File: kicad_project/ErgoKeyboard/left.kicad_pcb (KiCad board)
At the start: 2 copper layers, 163.8 x 116.3 mm, 58 parts

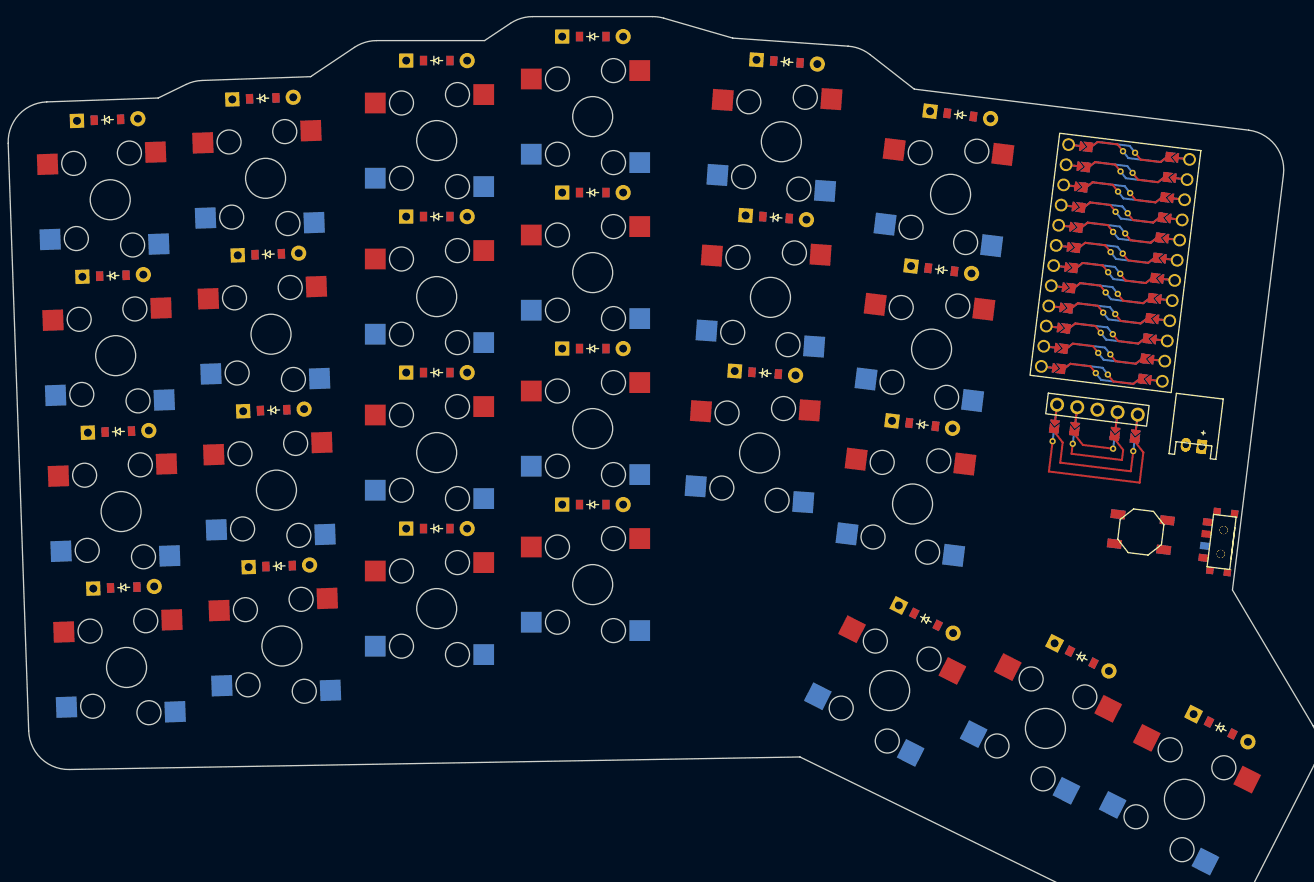
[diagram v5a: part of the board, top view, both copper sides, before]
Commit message: DRC doesn't like the smd trace hack, ouch
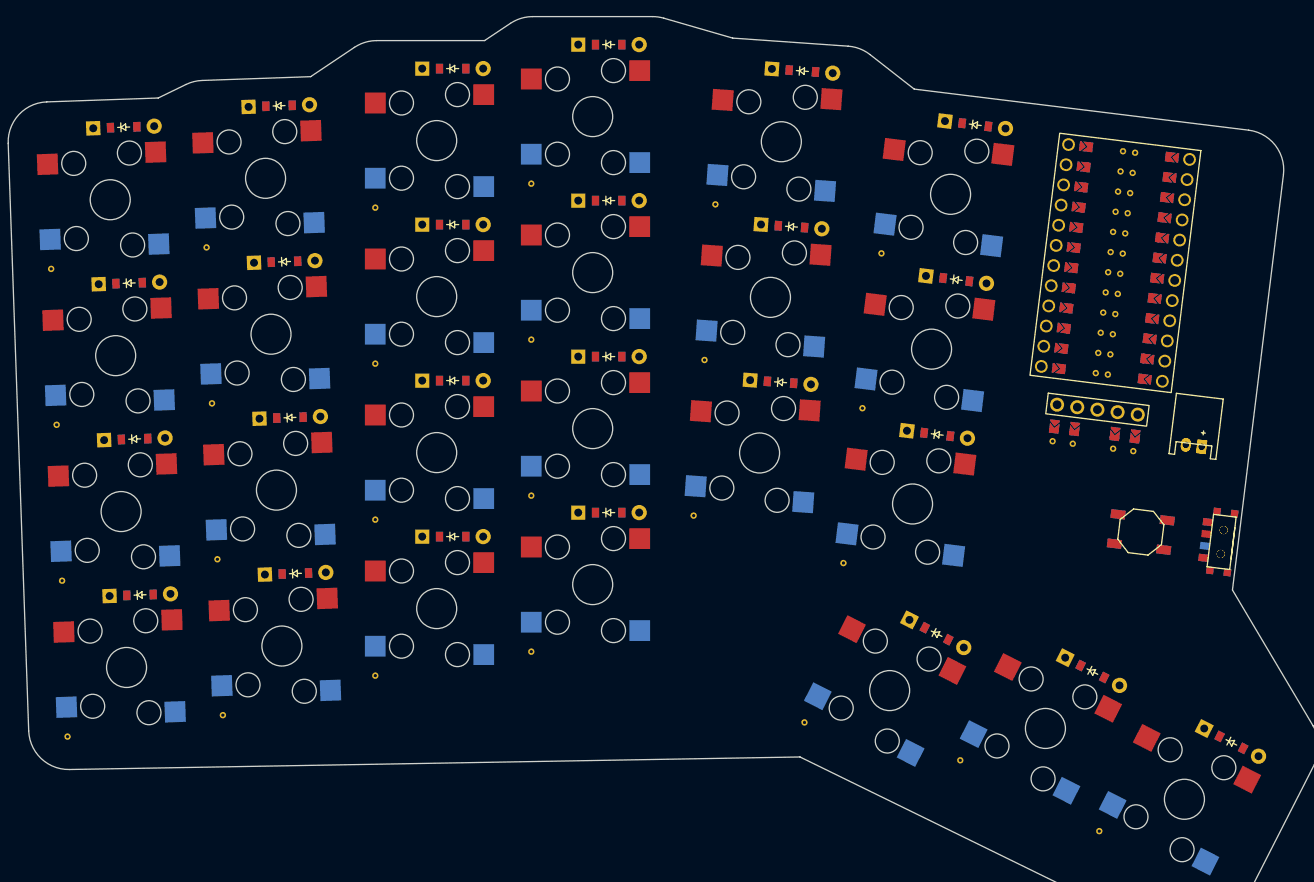
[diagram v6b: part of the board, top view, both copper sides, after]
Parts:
- moved D3 2.24 mm to (150.3, 127.0)
- moved D4 2.24 mm to (149.6, 107.5)
- moved D7 2.24 mm to (169.7, 124.3)
- moved D8 2.24 mm to (169.1, 104.8)
- moved D1 2.24 mm to (151.7, 165.9)
- moved D2 2.24 mm to (151.0, 146.4)
- moved D5 2.24 mm to (171.1, 163.3)
- moved D6 2.24 mm to (170.4, 143.8)
- moved D17 2.24 mm to (231.8, 139.4)
- moved D18 2.24 mm to (233.1, 119.9)
- moved D19 2.24 mm to (234.5, 100.4)
- moved D20 2.24 mm to (251.3, 145.9)
- moved D21 2.24 mm to (253.7, 126.5)
- moved D22 2.24 mm to (256.1, 107.2)
- moved D10 2.24 mm to (190.8, 139.1)
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
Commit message: using promicro pretty now, reverted some changes
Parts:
- MCU1: value rev_mcu -> (none); footprint revmicro -> ProMicro
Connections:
- MCU1 pad 1: P1 -> RAW
- MCU1 pad 10: P7 -> P14
- MCU1 pad 11: P8 -> P16
- MCU1 pad 12: P9 -> P10
- MCU1 pad 13: P10 -> P9
- MCU1 pad 14: P16 -> P8
- MCU1 pad 15: P14 -> P7
- MCU1 pad 16: P15 -> P6
- MCU1 pad 17: P18 -> P5
- MCU1 pad 18: P19 -> P4
- MCU1 pad 19: P20 -> P3
- MCU1 pad 2: P0 -> GND
- MCU1 pad 20: P21 -> P2
- MCU1 pad 21: VCC -> GND
- MCU1 pad 22: RST -> GND
- MCU1 pad 23: GND -> P0
- MCU1 pad 24: RAW -> P1
- MCU1 pad 3: GND -> RST
- MCU1 pad 4: GND -> VCC
- MCU1 pad 5: P2 -> P21
- MCU1 pad 6: P3 -> P20
- MCU1 pad 7: P4 -> P19
- MCU1 pad 8: P5 -> P18
- MCU1 pad 9: P6 -> P15

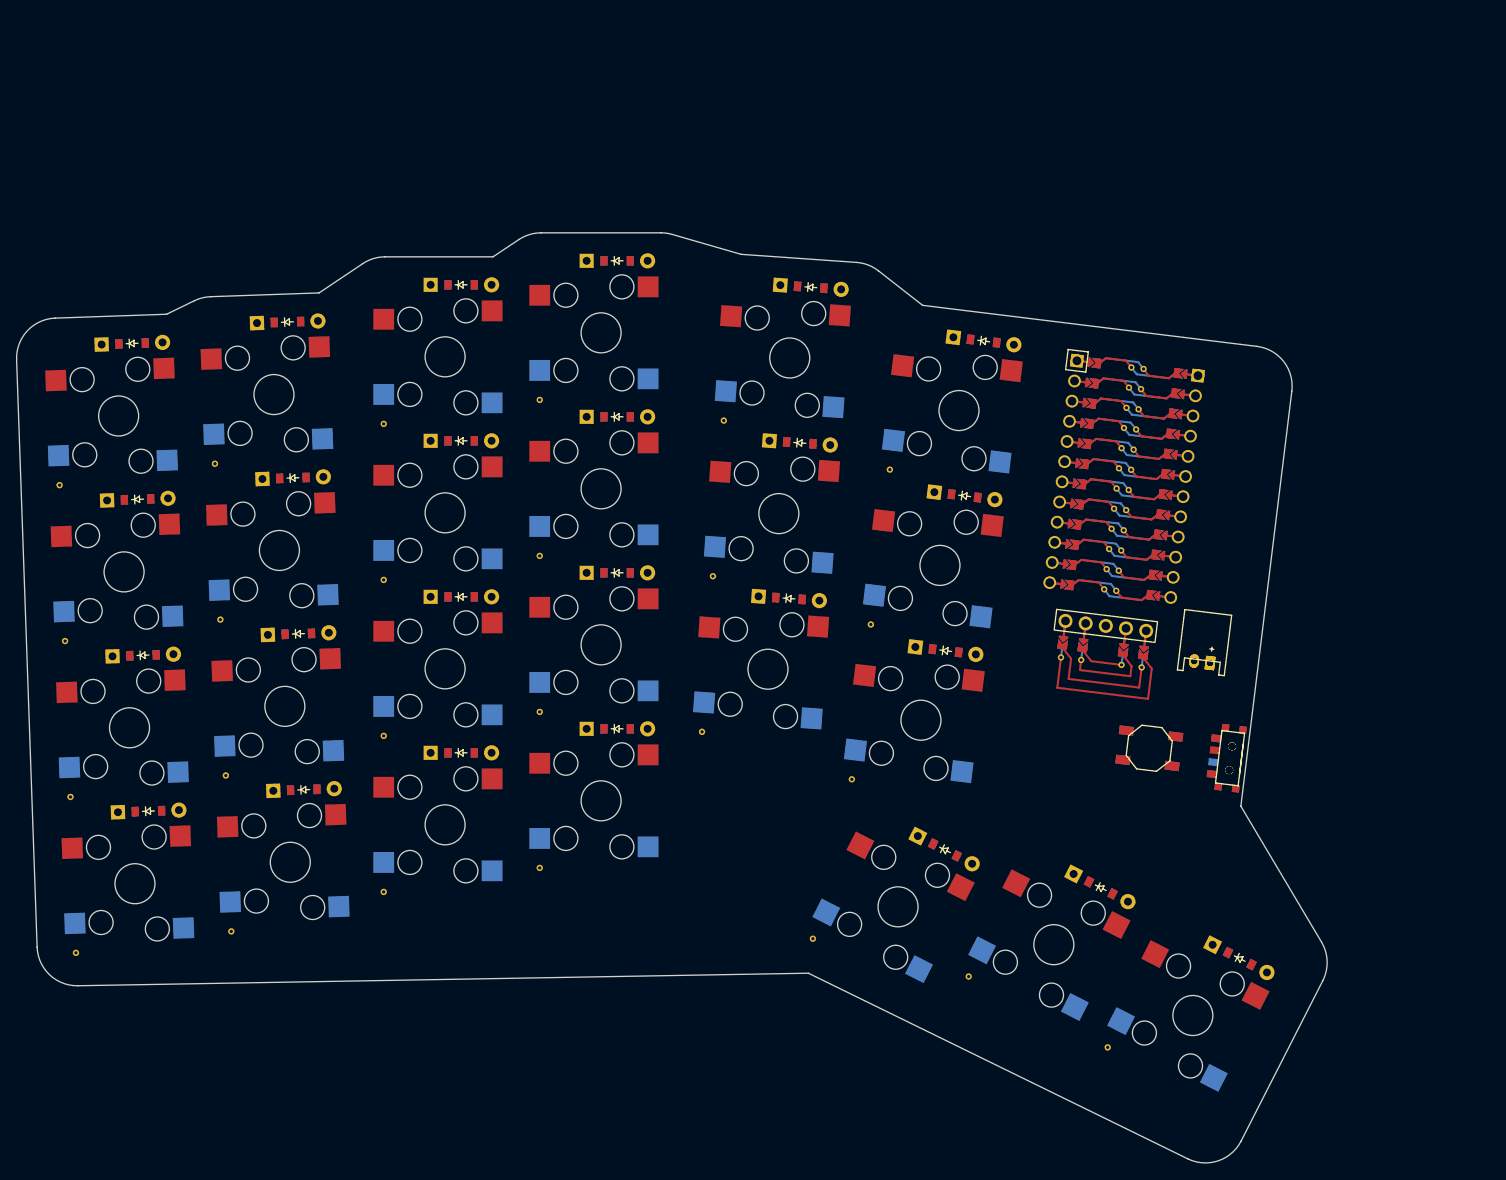
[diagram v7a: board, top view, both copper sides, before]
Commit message: niceview reworked to "pretty" method
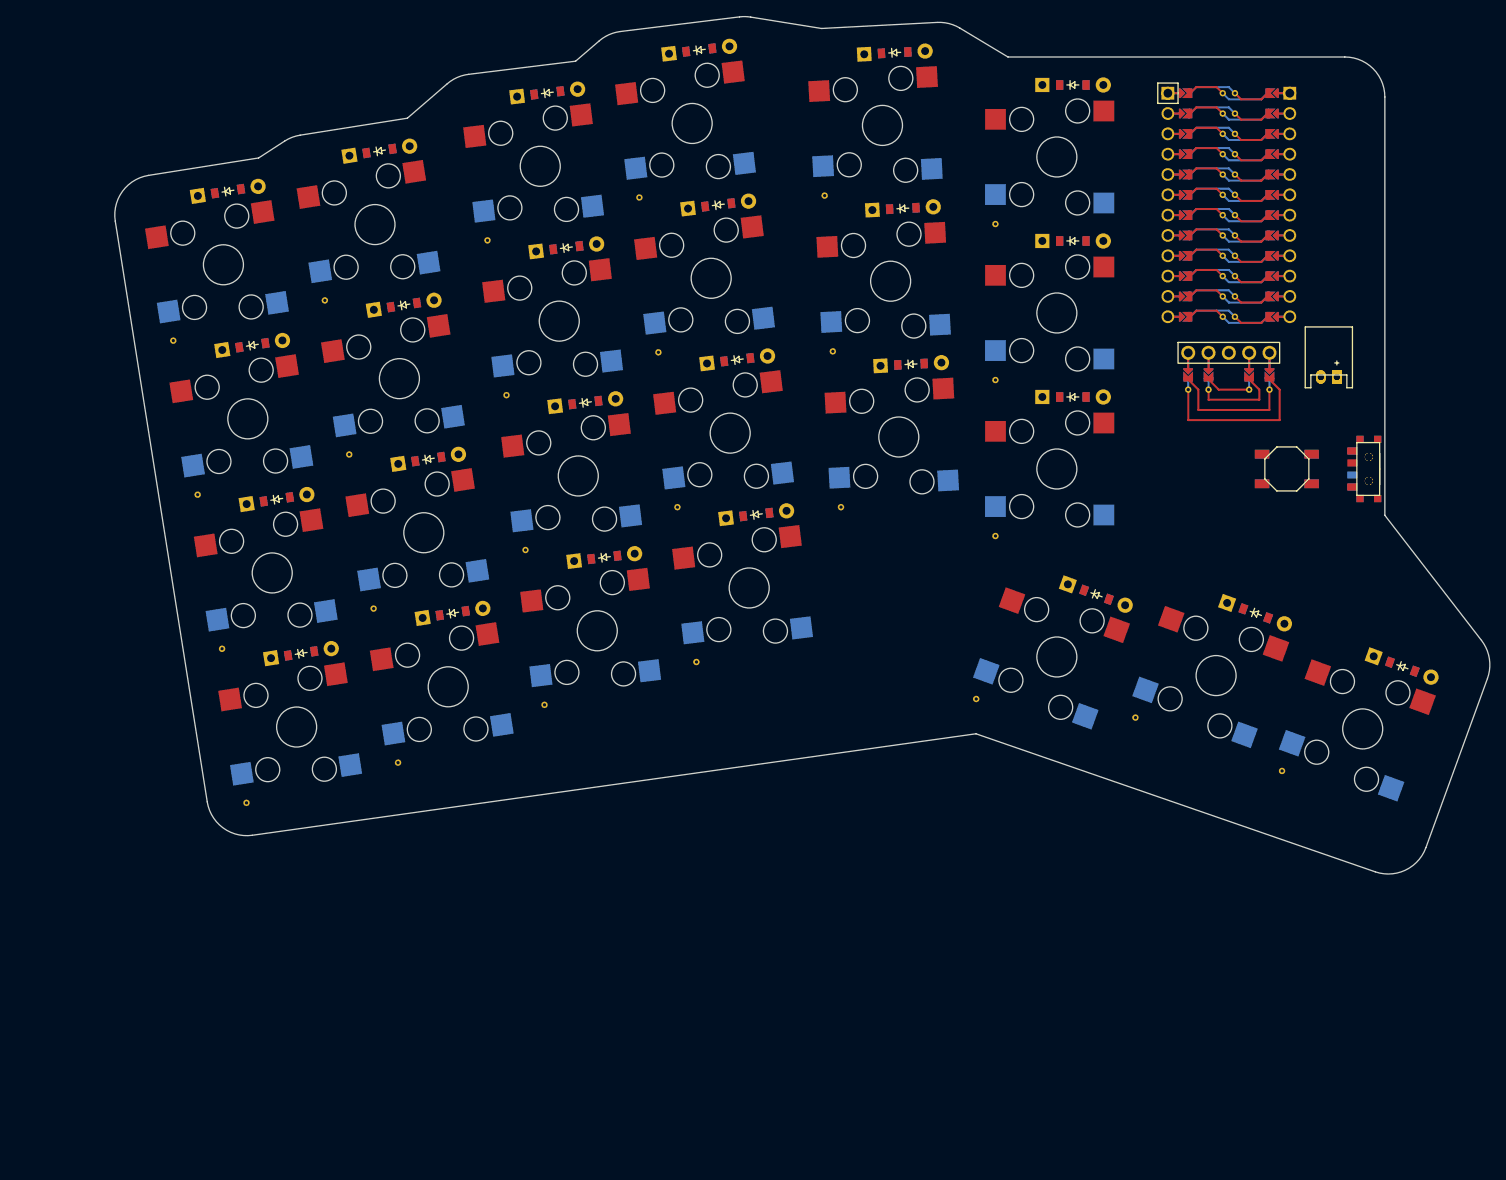
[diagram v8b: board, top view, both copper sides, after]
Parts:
- moved D25 41.8 mm to (308.4, 147.9), turned to -20 degrees
- moved S25 41.6 mm to (303.5, 155.7), turned to -20 degrees
- moved T1 40.1 mm to (304.2, 123.2), turned to -90 degrees
- moved T2 40.1 mm to (304.2, 123.2), turned to -90 degrees
- moved D24 39.4 mm to (290.1, 141.2), turned to -20 degrees
- moved S24 39.3 mm to (285.1, 149.0), turned to -20 degrees
- moved JST1 39.0 mm to (299.2, 111.7), turned to 180 degrees
- moved JST2 39.0 mm to (299.2, 111.7), turned to 180 degrees
- moved B1 38.9 mm to (294.0, 123.2), turned to 0 degrees
- moved B2 38.9 mm to (294.0, 123.2), turned to 0 degrees
- moved D23 37.1 mm to (270.2, 138.9), turned to -20 degrees
- moved S23 37.0 mm to (265.2, 146.7), turned to -20 degrees
- moved OLED1 36.8 mm to (286.7, 92.2), turned to 0 degrees
- moved MCU1 36.7 mm to (286.7, 90.2), turned to -90 degrees
- moved S20 35.7 mm to (265.2, 123.2), turned to 0 degrees
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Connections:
- OLED1 pad : P1 -> P2
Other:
- board size 163.8 x 116.3 mm -> 171.9 x 107.2 mm
